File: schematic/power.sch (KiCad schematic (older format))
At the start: 10 parts

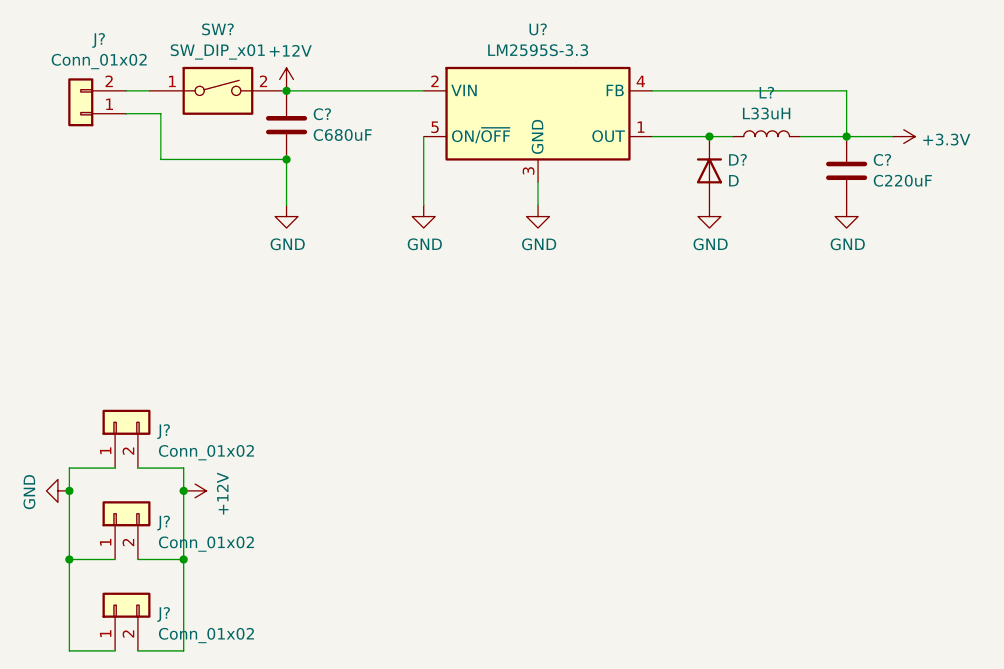
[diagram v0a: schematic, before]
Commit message: prototype footprint and placement test
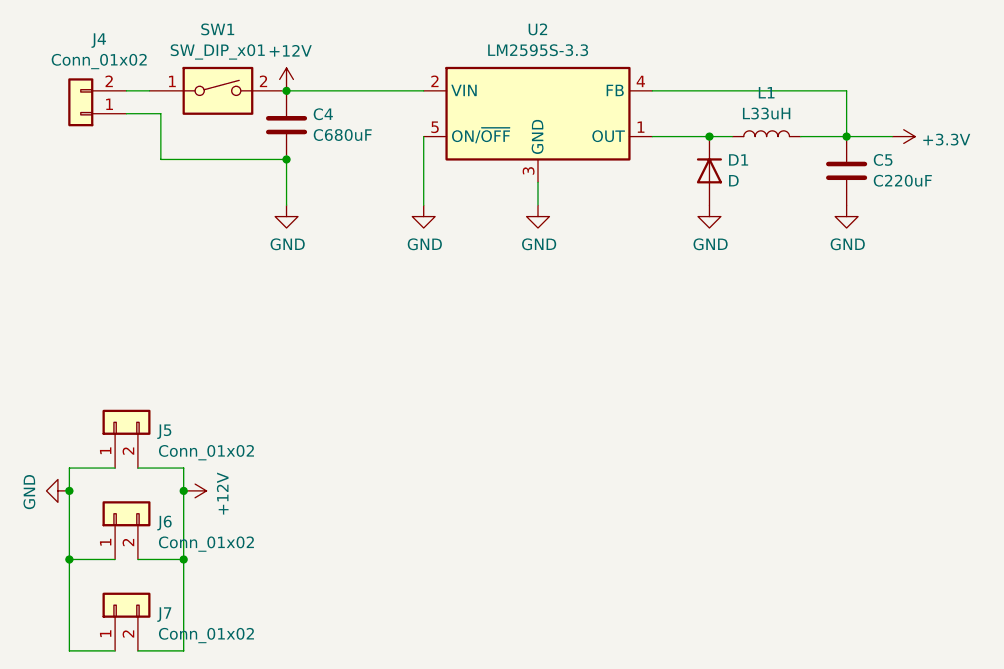
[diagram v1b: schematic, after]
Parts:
- C4, C5: renamed from C?; footprint (none) -> Capacitor_SMD:C_0805_2012Metric_Pad1.15x1.40mm_HandSolder
- D1: renamed from D?; footprint (none) -> Diode_SMD:D_0805_2012Metric_Castellated
- J4: renamed from J?; footprint (none) -> Connector_AMASS:AMASS_XT60-M_1x02_P7.20mm_Vertical
- J5, J6, J7: renamed from J?; footprint (none) -> Connector_AMASS:AMASS_XT60-F_1x02_P7.20mm_Vertical
- L1: renamed from L?; footprint (none) -> Inductor_SMD:L_1206_3216Metric_Pad1.42x1.75mm_HandSolder
- SW1: renamed from SW?; footprint (none) -> Button_Switch_THT:SW_MEC_5GTH9
- gave numbers to parts that had none: 1
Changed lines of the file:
@@
 P 3650 1950
 AR Path="/5EEDDF06" Ref="U?"  Part="1"
-AR Path="/5EEC6D97/5EEDDF06" Ref="U?"  Part="1"
-F 0 "U?" H 3650 2317 50  0000 C CNN
+AR Path="/5EEC6D97/5EEDDF06" Ref="U2"  Part="1"
+F 0 "U2" H 3650 2317 50  0000 C CNN
 F 1 "LM2595S-3.3" H 3650 2226 50  0000 C CNN
 F 2 "Package_TO_SOT_SMD:TO-263-5_TabPin3" H 3700 1700 50  0001 L CIN
@@
 P 2550 2350
 AR Path="/5EEDDF0C" Ref="#PWR?"  Part="1"
-AR Path="/5EEC6D97/5EEDDF0C" Ref="#PWR?"  Part="1"
-F 0 "#PWR?" H 2550 2100 50  0001 C CNN
+AR Path="/5EEC6D97/5EEDDF0C" Ref="#PWR022"  Part="1"
+F 0 "#PWR022" H 2550 2100 50  0001 C CNN
 F 1 "GND" H 2555 2177 50  0000 C CNN
 F 2 "" H 2550 2350 50  0001 C CNN
@@
 P 2550 1850
 AR Path="/5EEDDF12" Ref="#PWR?"  Part="1"
-AR Path="/5EEC6D97/5EEDDF12" Ref="#PWR?"  Part="1"
-F 0 "#PWR?" H 2550 1700 50  0001 C CNN
+AR Path="/5EEC6D97/5EEDDF12" Ref="#PWR021"  Part="1"
+F 0 "#PWR021" H 2550 1700 50  0001 C CNN
 F 1 "+12V" H 2565 2023 50  0000 C CNN
 F 2 "" H 2550 1850 50  0001 C CNN
@@
 P 5000 2200
 AR Path="/5EEDDF18" Ref="C?"  Part="1"
-AR Path="/5EEC6D97/5EEDDF18" Ref="C?"  Part="1"
-F 0 "C?" H 5115 2246 50  0000 L CNN
+AR Path="/5EEC6D97/5EEDDF18" Ref="C5"  Part="1"
+F 0 "C5" H 5115 2246 50  0000 L CNN
 F 1 "C220uF" H 5115 2155 50  0000 L CNN
-F 2 "" H 5038 2050 50  0001 C CNN
+F 2 "Capacitor_SMD:C_0805_2012Metric_Pad1.15x1.40mm_HandSolder" H 5038 2050 50  0001 C CNN
 F 3 "~" H 5000 2200 50  0001 C CNN
 	1    5000 2200
@@
 P 2550 2000
 AR Path="/5EEDDF1E" Ref="C?"  Part="1"
-AR Path="/5EEC6D97/5EEDDF1E" Ref="C?"  Part="1"
-F 0 "C?" H 2665 2046 50  0000 L CNN
+AR Path="/5EEC6D97/5EEDDF1E" Ref="C4"  Part="1"
+F 0 "C4" H 2665 2046 50  0000 L CNN
 F 1 "C680uF" H 2665 1955 50  0000 L CNN
-F 2 "" H 2588 1850 50  0001 C CNN
+F 2 "Capacitor_SMD:C_0805_2012Metric_Pad1.15x1.40mm_HandSolder" H 2588 1850 50  0001 C CNN
 F 3 "~" H 2550 2000 50  0001 C CNN
 	1    2550 2000
@@
 P 3150 2350
 AR Path="/5EEDDF26" Ref="#PWR?"  Part="1"
-AR Path="/5EEC6D97/5EEDDF26" Ref="#PWR?"  Part="1"
-F 0 "#PWR?" H 3150 2100 50  0001 C CNN
+AR Path="/5EEC6D97/5EEDDF26" Ref="#PWR023"  Part="1"
+F 0 "#PWR023" H 3150 2100 50  0001 C CNN
 F 1 "GND" H 3155 2177 50  0000 C CNN
 F 2 "" H 3150 2350 50  0001 C CNN
@@
 P 3650 2350
 AR Path="/5EEDDF2C" Ref="#PWR?"  Part="1"
-AR Path="/5EEC6D97/5EEDDF2C" Ref="#PWR?"  Part="1"
-F 0 "#PWR?" H 3650 2100 50  0001 C CNN
+AR Path="/5EEC6D97/5EEDDF2C" Ref="#PWR024"  Part="1"
+F 0 "#PWR024" H 3650 2100 50  0001 C CNN
 F 1 "GND" H 3655 2177 50  0000 C CNN
 F 2 "" H 3650 2350 50  0001 C CNN
@@
 P 4400 2200
 AR Path="/5EEDDF32" Ref="D?"  Part="1"
-AR Path="/5EEC6D97/5EEDDF32" Ref="D?"  Part="1"
-F 0 "D?" V 4354 2279 50  0000 L CNN
+AR Path="/5EEC6D97/5EEDDF32" Ref="D1"  Part="1"
+F 0 "D1" V 4354 2279 50  0000 L CNN
 F 1 "D" V 4445 2279 50  0000 L CNN
-F 2 "" H 4400 2200 50  0001 C CNN
+F 2 "Diode_SMD:D_0805_2012Metric_Castellated" H 4400 2200 50  0001 C CNN
 F 3 "~" H 4400 2200 50  0001 C CNN
 	1    4400 2200
@@
 P 4650 2050
 AR Path="/5EEDDF38" Ref="L?"  Part="1"
-AR Path="/5EEC6D97/5EEDDF38" Ref="L?"  Part="1"
-F 0 "L?" V 4840 2050 50  0000 C CNN
+AR Path="/5EEC6D97/5EEDDF38" Ref="L1"  Part="1"
+F 0 "L1" V 4840 2050 50  0000 C CNN
 F 1 "L33uH" V 4749 2050 50  0000 C CNN
-F 2 "" H 4650 2050 50  0001 C CNN
+F 2 "Inductor_SMD:L_1206_3216Metric_Pad1.42x1.75mm_HandSolder" H 4650 2050 50  0001 C CNN
 F 3 "~" H 4650 2050 50  0001 C CNN
 	1    4650 2050
@@
 P 4400 2350
 AR Path="/5EEDDF3E" Ref="#PWR?"  Part="1"
-AR Path="/5EEC6D97/5EEDDF3E" Ref="#PWR?"  Part="1"
-F 0 "#PWR?" H 4400 2100 50  0001 C CNN
+AR Path="/5EEC6D97/5EEDDF3E" Ref="#PWR025"  Part="1"
+F 0 "#PWR025" H 4400 2100 50  0001 C CNN
 F 1 "GND" H 4405 2177 50  0000 C CNN
 F 2 "" H 4400 2350 50  0001 C CNN
@@
 P 5000 2350
 AR Path="/5EEDDF44" Ref="#PWR?"  Part="1"
-AR Path="/5EEC6D97/5EEDDF44" Ref="#PWR?"  Part="1"
-F 0 "#PWR?" H 5000 2100 50  0001 C CNN
+AR Path="/5EEC6D97/5EEDDF44" Ref="#PWR026"  Part="1"
+F 0 "#PWR026" H 5000 2100 50  0001 C CNN
 F 1 "GND" H 5005 2177 50  0000 C CNN
 F 2 "" H 5000 2350 50  0001 C CNN
@@
 P 5200 2050
 AR Path="/5EEDDF4A" Ref="#PWR?"  Part="1"
-AR Path="/5EEC6D97/5EEDDF4A" Ref="#PWR?"  Part="1"
-F 0 "#PWR?" H 5200 1900 50  0001 C CNN
+AR Path="/5EEC6D97/5EEDDF4A" Ref="#PWR027"  Part="1"
+F 0 "#PWR027" H 5200 1900 50  0001 C CNN
 F 1 "+3.3V" V 5215 2178 50  0000 L CNN
 F 2 "" H 5200 2050 50  0001 C CNN
@@
 P 1650 1950
 AR Path="/5EEDDF5E" Ref="J?"  Part="1"
-AR Path="/5EEC6D97/5EEDDF5E" Ref="J?"  Part="1"
-F 0 "J?" H 1568 1625 50  0000 C CNN
+AR Path="/5EEC6D97/5EEDDF5E" Ref="J4"  Part="1"
+F 0 "J4" H 1568 1625 50  0000 C CNN
 F 1 "Conn_01x02" H 1568 1716 50  0000 C CNN
-F 2 "" H 1650 1950 50  0001 C CNN
+F 2 "Connector_AMASS:AMASS_XT60-M_1x02_P7.20mm_Vertical" H 1650 1950 50  0001 C CNN
 F 3 "~" H 1650 1950 50  0001 C CNN
 	1    1650 1950
@@
 P 2250 1850
 AR Path="/5EEDDF64" Ref="SW?"  Part="1"
-AR Path="/5EEC6D97/5EEDDF64" Ref="SW?"  Part="1"
-F 0 "SW?" H 2250 2117 50  0000 C CNN
+AR Path="/5EEC6D97/5EEDDF64" Ref="SW1"  Part="1"
+F 0 "SW1" H 2250 2117 50  0000 C CNN
 F 1 "SW_DIP_x01" H 2250 2026 50  0000 C CNN
-F 2 "" H 2250 1850 50  0001 C CNN
+F 2 "Button_Switch_THT:SW_MEC_5GTH9" H 2250 1850 50  0001 C CNN
 F 3 "~" H 2250 1850 50  0001 C CNN
 	1    2250 1850
@@
 P 1800 3300
 AR Path="/5EEFF2E3" Ref="J?"  Part="1"
-AR Path="/5EEC6D97/5EEFF2E3" Ref="J?"  Part="1"
-F 0 "J?" V 1764 3112 50  0000 R CNN
+AR Path="/5EEC6D97/5EEFF2E3" Ref="J5"  Part="1"
+F 0 "J5" V 1764 3112 50  0000 R CNN
 F 1 "Conn_01x02" V 1673 3112 50  0000 R CNN
-F 2 "" H 1800 3300 50  0001 C CNN
+F 2 "Connector_AMASS:AMASS_XT60-F_1x02_P7.20mm_Vertical" H 1800 3300 50  0001 C CNN
 F 3 "~" H 1800 3300 50  0001 C CNN
 	1    1800 3300
@@
 P 1800 3700
 AR Path="/5EEFF2E9" Ref="J?"  Part="1"
-AR Path="/5EEC6D97/5EEFF2E9" Ref="J?"  Part="1"
-F 0 "J?" V 1764 3512 50  0000 R CNN
+AR Path="/5EEC6D97/5EEFF2E9" Ref="J6"  Part="1"
+F 0 "J6" V 1764 3512 50  0000 R CNN
 F 1 "Conn_01x02" V 1673 3512 50  0000 R CNN
-F 2 "" H 1800 3700 50  0001 C CNN
+F 2 "Connector_AMASS:AMASS_XT60-F_1x02_P7.20mm_Vertical" H 1800 3700 50  0001 C CNN
 F 3 "~" H 1800 3700 50  0001 C CNN
 	1    1800 3700
@@
 P 1800 4100
 AR Path="/5EEFF2EF" Ref="J?"  Part="1"
-AR Path="/5EEC6D97/5EEFF2EF" Ref="J?"  Part="1"
-F 0 "J?" V 1764 3912 50  0000 R CNN
+AR Path="/5EEC6D97/5EEFF2EF" Ref="J7"  Part="1"
+F 0 "J7" V 1764 3912 50  0000 R CNN
 F 1 "Conn_01x02" V 1673 3912 50  0000 R CNN
-F 2 "" H 1800 4100 50  0001 C CNN
+F 2 "Connector_AMASS:AMASS_XT60-F_1x02_P7.20mm_Vertical" H 1800 4100 50  0001 C CNN
 F 3 "~" H 1800 4100 50  0001 C CNN
 	1    1800 4100
@@
 P 2100 3600
 AR Path="/5EEFF301" Ref="#PWR?"  Part="1"
-AR Path="/5EEC6D97/5EEFF301" Ref="#PWR?"  Part="1"
-F 0 "#PWR?" H 2100 3450 50  0001 C CNN
+AR Path="/5EEC6D97/5EEFF301" Ref="#PWR020"  Part="1"
+F 0 "#PWR020" H 2100 3450 50  0001 C CNN
 F 1 "+12V" H 2115 3773 50  0000 C CNN
 F 2 "" H 2100 3600 50  0001 C CNN
@@
 P 1600 3600
 AR Path="/5EEFF309" Ref="#PWR?"  Part="1"
-AR Path="/5EEC6D97/5EEFF309" Ref="#PWR?"  Part="1"
-F 0 "#PWR?" H 1600 3350 50  0001 C CNN
+AR Path="/5EEC6D97/5EEFF309" Ref="#PWR019"  Part="1"
+F 0 "#PWR019" H 1600 3350 50  0001 C CNN
 F 1 "GND" H 1605 3427 50  0000 C CNN
 F 2 "" H 1600 3600 50  0001 C CNN

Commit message: power on seperate board
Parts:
- added J5, J8: Conn_02x06_Odd_Even, Connector_IDC:IDC-Header_2x06_P2.54mm_Vertical, symbol Connector_Generic:Conn_02x06_Odd_Even
- added J6, J7: Conn_01x02, Connector_JST:JST_XH_B2B-XH-A_1x02_P2.50mm_Vertical, symbol Connector_Generic:Conn_01x02
- renumbered C4 to C1, C5 to C2, J4 to J1, J5 to J2, J6 to J3, J7 to J4, U2 to U1
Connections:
- net +3V3: now also J5.2 (Pin_2), J6.1 (Pin_1), J7.1 (Pin_1), J8.2 (Pin_2)
- net GND: now also J5.1 (Pin_1), J6.2 (Pin_2), J7.2 (Pin_2), J8.1 (Pin_1)
- new net I2C-SCL: J5.4 (Pin_4), J8.4 (Pin_4)
- new net I2C-SDA: J5.3 (Pin_3), J8.3 (Pin_3)
- new net RS485-A: J5.5 (Pin_5), J8.5 (Pin_5)
- new net RS485-B: J5.6 (Pin_6), J8.6 (Pin_6)
- new net SPI-MISO: J5.9 (Pin_9), J8.9 (Pin_9)
- new net SPI-MOSI: J5.7 (Pin_7), J8.7 (Pin_7)
- new net SPI-SCLK: J5.8 (Pin_8), J8.8 (Pin_8)
- new net SPI-SS0: J5.10 (Pin_10), J8.10 (Pin_10)
- new net SPI-SS1: J5.11 (Pin_11), J8.11 (Pin_11)
- new net SPI-SS2: J5.12 (Pin_12), J8.12 (Pin_12)

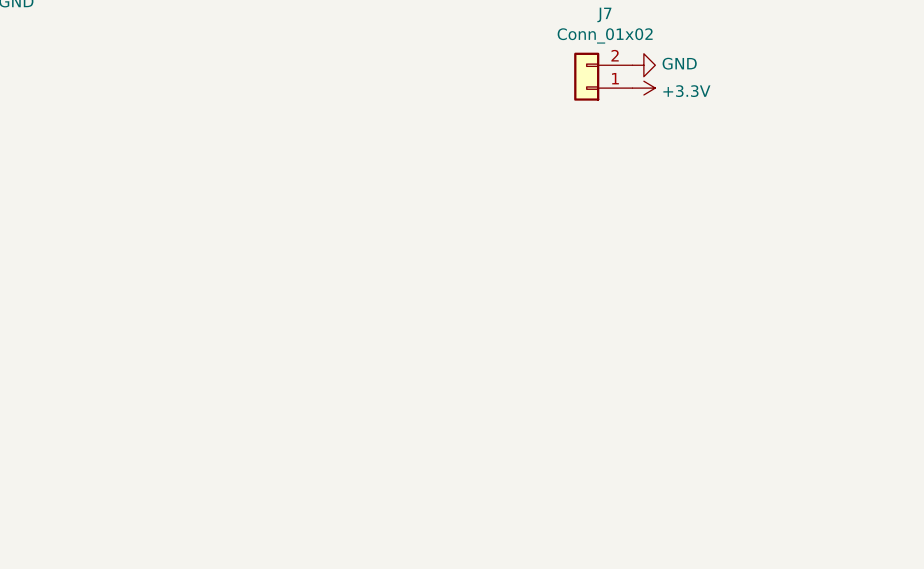
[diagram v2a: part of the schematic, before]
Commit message: added 5v boost converter
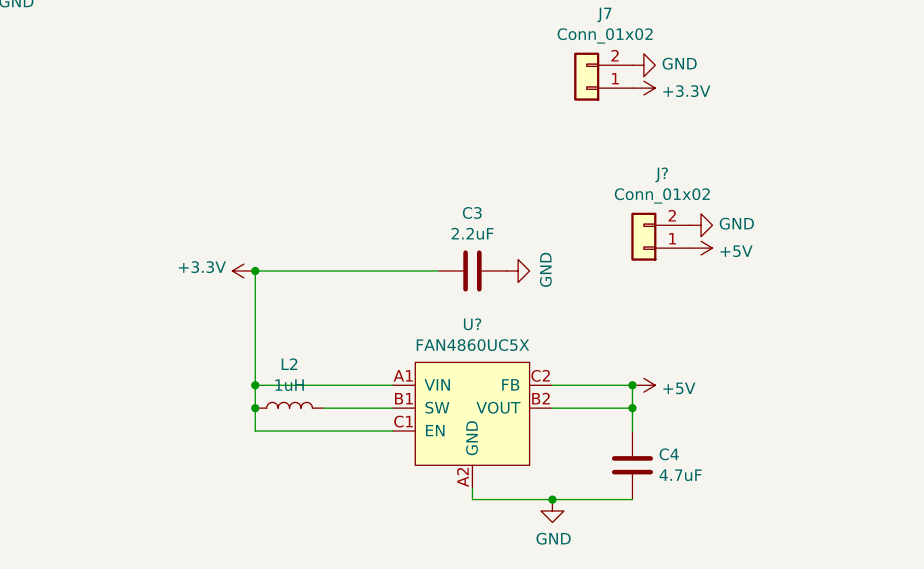
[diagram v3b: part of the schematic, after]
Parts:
- added C3: 2.2uF, symbol Device:C
- added C4: 4.7uF, symbol Device:C
- added J?: Conn_01x02, Connector_JST:JST_XH_B2B-XH-A_1x02_P2.50mm_Vertical, symbol Connector_Generic:Conn_01x02
- added L2: 1uH, symbol Device:L
- added U?: FAN4860UC5X, Package_CSP:WLCSP-6_1.4x1.0mm_P0.4mm, symbol Apsu_Library:FAN4860UC5X
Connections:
- net +3V3: now also C3.2, L2.1, U?.A1 (VIN), U?.C1 (EN)
- net GND: now also C3.1, C4.2, J?.2 (Pin_2), U?.A2 (GND)
- new net: L2.2, U?.B1 (SW)
- new net +5V: C4.1, J?.1 (Pin_1), U?.B2 (VOUT), U?.C2 (FB)
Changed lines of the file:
@@
+	0    1    1    0
+$EndComp
+$Comp
+L Device:C C3
+U 1 1 5EEDBA3F
+P 7000 3700
+F 0 "C3" V 6748 3700 50  0000 C CNN
+F 1 "2.2uF" V 6839 3700 50  0000 C CNN
+F 2 "" H 7038 3550 50  0001 C CNN
+F 3 "~" H 7000 3700 50  0001 C CNN
+	1    7000 3700
+	0    1    1    0
+$EndComp
+$Comp
+L Device:L L2
+U 1 1 5EEDC217
+P 6200 4300
+F 0 "L2" V 6390 4300 50  0000 C CNN
+F 1 "1uH" V 6299 4300 50  0000 C CNN
+F 2 "" H 6200 4300 50  0001 C CNN
+F 3 "~" H 6200 4300 50  0001 C CNN
+	1    6200 4300
+	0    -1   -1   0
+$EndComp
+$Comp
+L Device:C C4
+U 1 1 5EEDCB53
+P 7700 4550
+F 0 "C4" H 7815 4596 50  0000 L CNN
+F 1 "4.7uF" H 7815 4505 50  0000 L CNN
+F 2 "" H 7738 4400 50  0001 C CNN
+F 3 "~" H 7700 4550 50  0001 C CNN
+	1    7700 4550
+	1    0    0    -1
+$EndComp
+$Comp
+L power:+3.3V #PWR0118
+U 1 1 5EEDDCE0
+P 6050 3700
+F 0 "#PWR0118" H 6050 3550 50  0001 C CNN
+F 1 "+3.3V" V 6065 3828 50  0000 L CNN
+F 2 "" H 6050 3700 50  0001 C CNN
+F 3 "" H 6050 3700 50  0001 C CNN
+	1    6050 3700
+	0    -1   -1   0
+$EndComp
+Wire Wire Line
+	6350 4300 6650 4300
+Wire Wire Line
+	6650 4200 6050 4200
+Wire Wire Line
+	6050 4200 6050 4300
+Wire Wire Line
+	6050 3700 6050 4200
+Connection ~ 6050 4200
+Wire Wire Line
+	6050 3700 6850 3700
+Connection ~ 6050 3700
+Wire Wire Line
+	7350 4300 7700 4300
+Wire Wire Line
+	7700 4300 7700 4400
+Wire Wire Line
+	7350 4200 7700 4200
+Wire Wire Line
+	7700 4200 7700 4300
+Connection ~ 7700 4300
+Wire Wire Line
+	7000 4650 7000 4700
+Wire Wire Line
+	7000 4700 7350 4700
+$Comp
+L power:GND #PWR0119
+U 1 1 5EEECD72
+P 7350 4700
+AR Path="/5EEECD72" Ref="#PWR0119"  Part="1"
+AR Path="/5EEC6D97/5EEECD72" Ref="#PWR?"  Part="1"
+F 0 "#PWR0119" H 7350 4450 50  0001 C CNN
+F 1 "GND" H 7355 4527 50  0000 C CNN
+F 2 "" H 7350 4700 50  0001 C CNN
+F 3 "" H 7350 4700 50  0001 C CNN
+	1    7350 4700
+	1    0    0    -1
+$EndComp
+Connection ~ 7350 4700
+Wire Wire Line
+	7350 4700 7700 4700
+$Comp
+L power:GND #PWR0120
+U 1 1 5EEED207
+P 7150 3700
+AR Path="/5EEED207" Ref="#PWR0120"  Part="1"
+AR Path="/5EEC6D97/5EEED207" Ref="#PWR?"  Part="1"
+F 0 "#PWR0120" H 7150 3450 50  0001 C CNN
+F 1 "GND" H 7155 3527 50  0000 C CNN
+F 2 "" H 7150 3700 50  0001 C CNN
+F 3 "" H 7150 3700 50  0001 C CNN
+	1    7150 3700
+	0    -1   -1   0
+$EndComp
+$Comp
+L power:+5V #PWR0121
+U 1 1 5EEF0CAD
+P 7700 4200
+F 0 "#PWR0121" H 7700 4050 50  0001 C CNN
+F 1 "+5V" V 7715 4328 50  0000 L CNN
+F 2 "" H 7700 4200 50  0001 C CNN
+F 3 "" H 7700 4200 50  0001 C CNN
+	1    7700 4200
+	0    1    1    0
+$EndComp
+Connection ~ 7700 4200
+$Comp
+L Apsu_Library:FAN4860UC5X U?
+U 1 1 5EEDF879
+P 7000 4000
+F 0 "U?" H 7000 4065 50  0000 C CNN
+F 1 "FAN4860UC5X" H 7000 3974 50  0000 C CNN
+F 2 "Package_CSP:WLCSP-6_1.4x1.0mm_P0.4mm" H 7000 4000 50  0001 C CNN
+F 3 "https://datasheet.octopart.com/FAN4860UC5X-ON-Semiconductor-datasheet-137329910.pdf" H 7000 4000 50  0001 C CNN
+	1    7000 4000
+	1    0    0    -1
+$EndComp
+Wire Wire Line
+	6650 4400 6050 4400
+Wire Wire Line
+	6050 4400 6050 4300
+Connection ~ 6050 4300
+$Comp
+L Connector_Generic:Conn_01x02 J?
+U 1 1 5EEE4E8B
+P 7750 3600
+F 0 "J?" H 7668 3275 50  0000 C CNN
+F 1 "Conn_01x02" H 7668 3366 50  0000 C CNN
+F 2 "Connector_JST:JST_XH_B2B-XH-A_1x02_P2.50mm_Vertical" H 7750 3600 50  0001 C CNN
+F 3 "~" H 7750 3600 50  0001 C CNN
+	1    7750 3600
+	-1   0    0    1
+$EndComp
+$Comp
+L power:GND #PWR?
+U 1 1 5EEE57C2
+P 7950 3500
+F 0 "#PWR?" H 7950 3250 50  0001 C CNN
+F 1 "GND" V 7955 3372 50  0000 R CNN
+F 2 "" H 7950 3500 50  0001 C CNN
+F 3 "" H 7950 3500 50  0001 C CNN
+	1    7950 3500
+	0    -1   -1   0
+$EndComp
+$Comp
+L power:+5V #PWR?
+U 1 1 5EEE5D54
+P 7950 3600
+F 0 "#PWR?" H 7950 3450 50  0001 C CNN
+F 1 "+5V" V 7965 3728 50  0000 L CNN
+F 2 "" H 7950 3600 50  0001 C CNN
+F 3 "" H 7950 3600 50  0001 C CNN
+	1    7950 3600
 	0    1    1    0
 $EndComp
